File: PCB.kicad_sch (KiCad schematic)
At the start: 29 parts

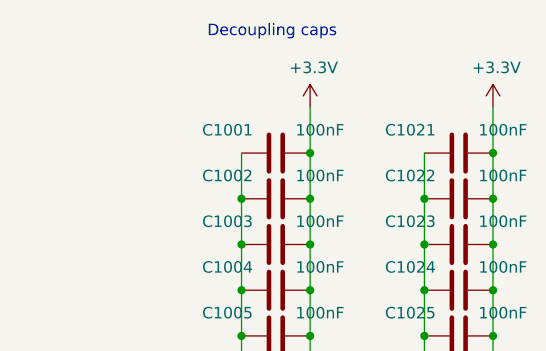
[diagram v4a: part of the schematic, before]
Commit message: Go back to ISO1050 for CAN transceiver
Also add CAN RX and TX LEDs and beef up buck capacitors
as much as space allows.
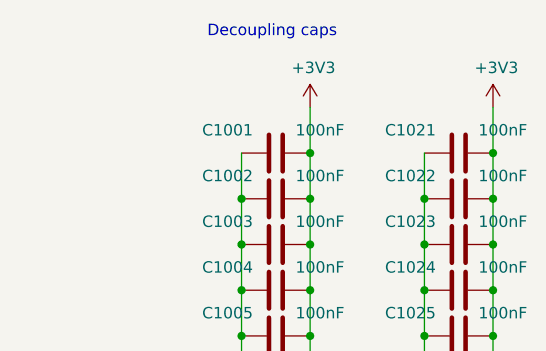
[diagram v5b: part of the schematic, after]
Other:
- company: Hat Labs Ltd -> Hat Labs Oy
- title: Sailor Hat with ESP32 -> SH-ESP32

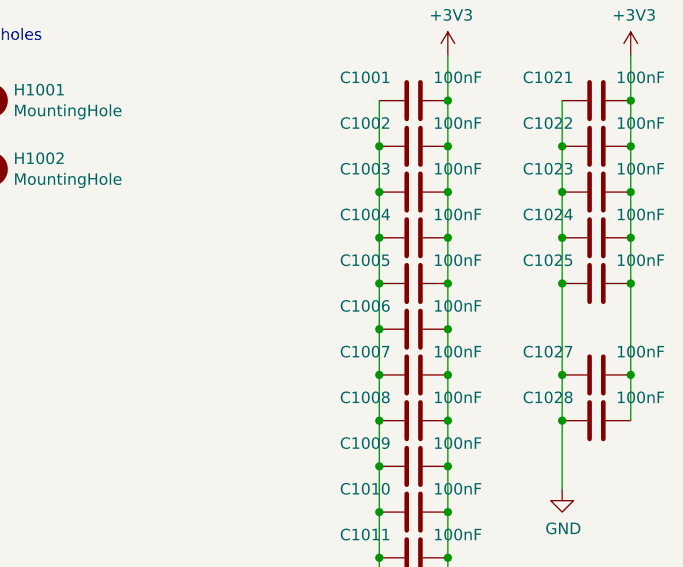
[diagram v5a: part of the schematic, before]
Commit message: Change buck converter to LMR54410
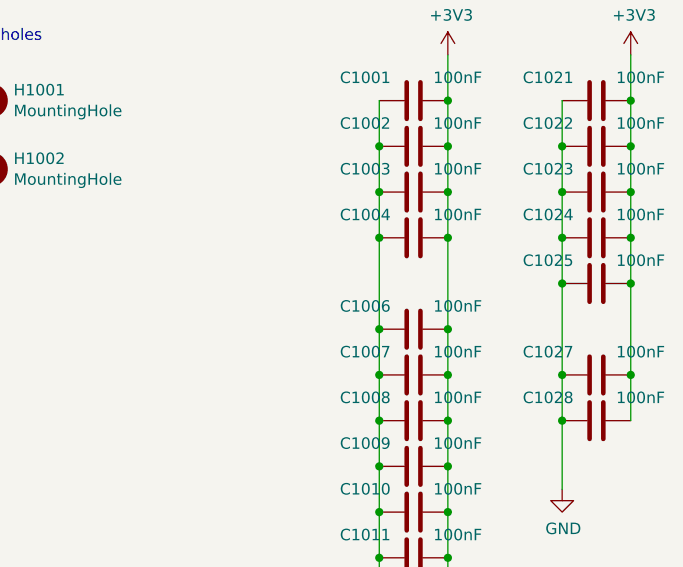
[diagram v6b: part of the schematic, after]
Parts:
- removed C1005: 100nF, Capacitor_SMD:C_0402_1005Metric, symbol Device:C
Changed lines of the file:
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@@
 	(title_block
 		(title "SH-ESP32")
-		(date "2024-06-27")
-		(rev "2.1.0")
+		(date "2024-09-24")
+		(rev "2.2.0")
 		(company "Hat Labs Oy")
 		(comment 1 "https://creativecommons.org/licenses/by-sa/4.0")
@@
 	)
 	(junction
-		(at 91.44 67.31)
-		(diameter 0)
-		(color 0 0 0 0)
-	)
-	(junction
 		(at 91.44 143.51)
 		(diameter 0)
@@
 	)
 	(junction
-		(at 99.06 67.31)
-		(diameter 0)
-		(color 0 0 0 0)
-	)
-	(junction
 		(at 111.76 62.23)
 		(diameter 0)
@@
 	(wire
 		(pts
-			(xy 99.06 67.31) (xy 99.06 62.23)
-		)
-		(stroke
-			(width 0)
-			(type default)
-		)
-	)
-	(wire
-		(pts
 			(xy 91.44 128.27) (xy 91.44 133.35)
 		)
@@
 	(wire
 		(pts
-			(xy 91.44 67.31) (xy 91.44 72.39)
+			(xy 91.44 62.23) (xy 91.44 72.39)
 		)
 		(stroke
@@
 	(wire
 		(pts
-			(xy 91.44 62.23) (xy 91.44 67.31)
-		)
-		(stroke
-			(width 0)
-			(type default)
-		)
-	)
-	(wire
-		(pts
-			(xy 99.06 72.39) (xy 99.06 67.31)
+			(xy 99.06 62.23) (xy 99.06 72.39)
 		)
 		(stroke
@@
 	(symbol
 		(lib_id "Device:C")
-		(at 95.25 67.31 90)
-		(mirror x)
-		(unit 1)
-		(exclude_from_sim no)
-		(in_bom yes)
-		(on_board yes)
-		(dnp no)
-		(property "Reference" "C1005"
-			(at 92.71 64.77 90)
-			(effects
-				(font
-					(size 1.27 1.27)
-				)
-				(justify left)
-			)
-		)
-		(property "Value" "100nF"
-			(at 102.87 64.77 90)
-			(effects
-				(font
-					(size 1.27 1.27)
-				)
-				(justify left)
-			)
-		)
-		(property "Footprint" "Capacitor_SMD:C_0402_1005Metric"
-			(at 99.06 68.2752 0)
-			(effects
-				(font
-					(size 1.27 1.27)
-				)
-				(hide yes)
-			)
-		)
-		(property "Datasheet" "~"
-			(at 95.25 67.31 0)
-			(effects
-				(font
-					(size 1.27 1.27)
-				)
-				(hide yes)
-			)
-		)
-		(property "Description" ""
-			(at 95.25 67.31 0)
-			(effects
-				(font
-					(size 1.27 1.27)
-				)
-				(hide yes)
-			)
-		)
-		(property "LCSC" "C1525"
-			(at 95.25 67.31 0)
-			(effects
-				(font
-					(size 1.27 1.27)
-				)
-				(hide yes)
-			)
-		)
-		(property "JLCPCB_CORRECTION" ""
-			(at 95.25 67.31 0)
-			(effects
-				(font
-					(size 1.27 1.27)
-				)
-				(hide yes)
-			)
-		)
-		(pin "1"
-		)
-		(pin "2"
-		)
-		(instances
-			(project "SH-ESP32"
-				(path "/dff502f1-2fe5-4c09-a767-aabc78c2e052/00000000-0000-0000-0000-00005fc0c355"
-					(reference "C1005")
-					(unit 1)
-				)
-			)
-		)
-	)
-	(symbol
-		(lib_id "Device:C")
 		(at 95.25 72.39 90)
 		(mirror x)
@@
 			)
 		)
-		(property "Description" ""
+		(property "Description" "Power symbol creates a global label with name \"+3.3V\""
 			(at 99.06 41.91 0)
 			(effects
@@
 			)
 		)
-		(property "Description" ""
+		(property "Description" "Power symbol creates a global label with name \"GND\" , ground"
 			(at 91.44 148.59 0)
 			(effects
@@
 			)
 		)
-		(property "Description" ""
+		(property "Description" "Power symbol creates a global label with name \"+3.3V\""
 			(at 119.38 41.91 0)
 			(effects
@@
 			)
 		)
-		(property "Description" ""
+		(property "Description" "Power symbol creates a global label with name \"GND\" , ground"
 			(at 111.76 90.17 0)
 			(effects
